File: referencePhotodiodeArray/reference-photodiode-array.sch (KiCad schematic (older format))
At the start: 18 parts

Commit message: fix reference photodiode array
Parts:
- D1, D2, D3, D4, D5, D6, D7, D8: footprint Diodes_ThroughHole:D_T-1_P5.08mm_Horizontal -> testPad:BPW34
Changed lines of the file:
@@
 F 0 "D2" H 2420 2370 50  0000 L CNN
 F 1 "D_Photo" H 2360 2190 50  0000 C CNN
-F 2 "Diodes_ThroughHole:D_T-1_P5.08mm_Horizontal" H 2350 2300 50  0001 C CNN
+F 2 "testPad:BPW34" H 2350 2300 50  0001 C CNN
 F 3 "" H 2350 2300 50  0000 C CNN
 	1    2400 2300
@@
 F 0 "D3" H 2870 1670 50  0000 L CNN
 F 1 "D_Photo" H 2810 1490 50  0000 C CNN
-F 2 "Diodes_ThroughHole:D_T-1_P5.08mm_Horizontal" H 2800 1600 50  0001 C CNN
+F 2 "testPad:BPW34" H 2800 1600 50  0001 C CNN
 F 3 "" H 2800 1600 50  0000 C CNN
 	1    2850 1600
@@
 F 0 "D1" H 2420 1670 50  0000 L CNN
 F 1 "D_Photo" H 2360 1490 50  0000 C CNN
-F 2 "Diodes_ThroughHole:D_T-1_P5.08mm_Horizontal" H 2350 1600 50  0001 C CNN
+F 2 "testPad:BPW34" H 2350 1600 50  0001 C CNN
 F 3 "" H 2350 1600 50  0000 C CNN
 	1    2400 1600
@@
 F 0 "D5" H 3320 1670 50  0000 L CNN
 F 1 "D_Photo" H 3260 1490 50  0000 C CNN
-F 2 "Diodes_ThroughHole:D_T-1_P5.08mm_Horizontal" H 3250 1600 50  0001 C CNN
+F 2 "testPad:BPW34" H 3250 1600 50  0001 C CNN
 F 3 "" H 3250 1600 50  0000 C CNN
 	1    3300 1600
@@
 F 0 "D7" H 3770 1670 50  0000 L CNN
 F 1 "D_Photo" H 3710 1490 50  0000 C CNN
-F 2 "Diodes_ThroughHole:D_T-1_P5.08mm_Horizontal" H 3700 1600 50  0001 C CNN
+F 2 "testPad:BPW34" H 3700 1600 50  0001 C CNN
 F 3 "" H 3700 1600 50  0000 C CNN
 	1    3750 1600
@@
 F 0 "D4" H 2870 2370 50  0000 L CNN
 F 1 "D_Photo" H 2810 2190 50  0000 C CNN
-F 2 "Diodes_ThroughHole:D_T-1_P5.08mm_Horizontal" H 2800 2300 50  0001 C CNN
+F 2 "testPad:BPW34" H 2800 2300 50  0001 C CNN
 F 3 "" H 2800 2300 50  0000 C CNN
 	1    2850 2300
@@
 F 0 "D6" H 3320 2370 50  0000 L CNN
 F 1 "D_Photo" H 3260 2190 50  0000 C CNN
-F 2 "Diodes_ThroughHole:D_T-1_P5.08mm_Horizontal" H 3250 2300 50  0001 C CNN
+F 2 "testPad:BPW34" H 3250 2300 50  0001 C CNN
 F 3 "" H 3250 2300 50  0000 C CNN
 	1    3300 2300
@@
 F 0 "D8" H 3770 2370 50  0000 L CNN
 F 1 "D_Photo" H 3710 2190 50  0000 C CNN
-F 2 "Diodes_ThroughHole:D_T-1_P5.08mm_Horizontal" H 3700 2300 50  0001 C CNN
+F 2 "testPad:BPW34" H 3700 2300 50  0001 C CNN
 F 3 "" H 3700 2300 50  0000 C CNN
 	1    3750 2300

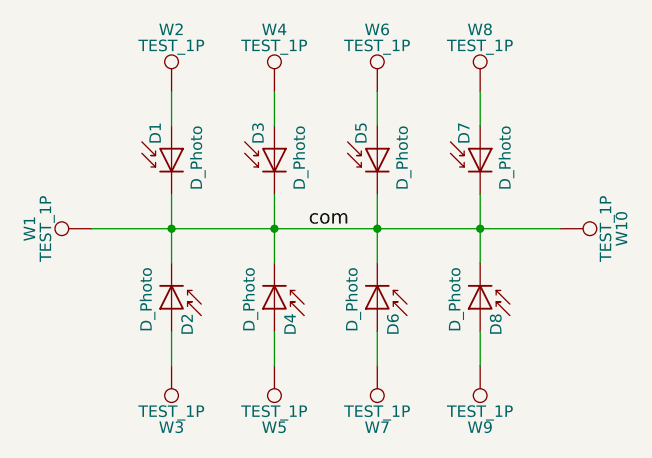
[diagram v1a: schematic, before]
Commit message: put pads on both sides
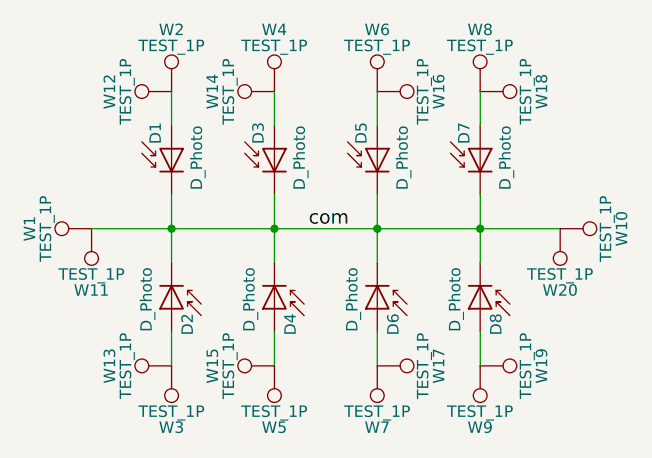
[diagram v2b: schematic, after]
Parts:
- added W11, W12, W13, W14, W15, W16, W17, W18, W19, W20: TEST_1P, testPad:SolderWirePad_single_SMD_5x2.3mm, symbol TEST_1P
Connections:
- net com: now also W11.1, W20.1
- net at D2.2 (A), W3.1: now also W13.1
- net at D3.2 (A), W4.1: now also W14.1
- net at D1.2 (A), W2.1: now also W12.1
- net at D5.2 (A), W6.1: now also W16.1
- net at D7.2 (A), W8.1: now also W18.1
- net at D4.2 (A), W5.1: now also W15.1
- net at D6.2 (A), W7.1: now also W17.1
- net at D8.2 (A), W9.1: now also W19.1
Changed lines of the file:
@@
 Text Label 3000 1950 0    60   ~ 0
 com
+$Comp
+L TEST_1P W12
+U 1 1 58C6E544
+P 2400 1350
+F 0 "W12" H 2400 1620 50  0000 C CNN
+F 1 "TEST_1P" H 2400 1550 50  0000 C CNN
+F 2 "testPad:SolderWirePad_single_SMD_5x2.3mm" H 2600 1350 50  0001 C CNN
+F 3 "" H 2600 1350 50  0000 C CNN
+	1    2400 1350
+	0    -1   -1   0
+$EndComp
+$Comp
+L TEST_1P W14
+U 1 1 58C6E5BF
+P 2850 1350
+F 0 "W14" H 2850 1620 50  0000 C CNN
+F 1 "TEST_1P" H 2850 1550 50  0000 C CNN
+F 2 "testPad:SolderWirePad_single_SMD_5x2.3mm" H 3050 1350 50  0001 C CNN
+F 3 "" H 3050 1350 50  0000 C CNN
+	1    2850 1350
+	0    -1   -1   0
+$EndComp
+$Comp
+L TEST_1P W16
+U 1 1 58C6E61B
+P 3300 1350
+F 0 "W16" H 3300 1620 50  0000 C CNN
+F 1 "TEST_1P" H 3300 1550 50  0000 C CNN
+F 2 "testPad:SolderWirePad_single_SMD_5x2.3mm" H 3500 1350 50  0001 C CNN
+F 3 "" H 3500 1350 50  0000 C CNN
+	1    3300 1350
+	0    1    1    0
+$EndComp
+$Comp
+L TEST_1P W18
+U 1 1 58C6E66E
+P 3750 1350
+F 0 "W18" H 3750 1620 50  0000 C CNN
+F 1 "TEST_1P" H 3750 1550 50  0000 C CNN
+F 2 "testPad:SolderWirePad_single_SMD_5x2.3mm" H 3950 1350 50  0001 C CNN
+F 3 "" H 3950 1350 50  0000 C CNN
+	1    3750 1350
+	0    1    1    0
+$EndComp
+$Comp
+L TEST_1P W19
+U 1 1 58C6E6C6
+P 3750 2550
+F 0 "W19" H 3750 2820 50  0000 C CNN
+F 1 "TEST_1P" H 3750 2750 50  0000 C CNN
+F 2 "testPad:SolderWirePad_single_SMD_5x2.3mm" H 3950 2550 50  0001 C CNN
+F 3 "" H 3950 2550 50  0000 C CNN
+	1    3750 2550
+	0    1    1    0
+$EndComp
+$Comp
+L TEST_1P W17
+U 1 1 58C6E721
+P 3300 2550
+F 0 "W17" H 3300 2820 50  0000 C CNN
+F 1 "TEST_1P" H 3300 2750 50  0000 C CNN
+F 2 "testPad:SolderWirePad_single_SMD_5x2.3mm" H 3500 2550 50  0001 C CNN
+F 3 "" H 3500 2550 50  0000 C CNN
+	1    3300 2550
+	0    1    1    0
+$EndComp
+$Comp
+L TEST_1P W15
+U 1 1 58C6E77F
+P 2850 2550
+F 0 "W15" H 2850 2820 50  0000 C CNN
+F 1 "TEST_1P" H 2850 2750 50  0000 C CNN
+F 2 "testPad:SolderWirePad_single_SMD_5x2.3mm" H 3050 2550 50  0001 C CNN
+F 3 "" H 3050 2550 50  0000 C CNN
+	1    2850 2550
+	0    -1   -1   0
+$EndComp
+$Comp
+L TEST_1P W13
+U 1 1 58C6E7F5
+P 2400 2550
+F 0 "W13" H 2400 2820 50  0000 C CNN
+F 1 "TEST_1P" H 2400 2750 50  0000 C CNN
+F 2 "testPad:SolderWirePad_single_SMD_5x2.3mm" H 2600 2550 50  0001 C CNN
+F 3 "" H 2600 2550 50  0000 C CNN
+	1    2400 2550
+	0    -1   -1   0
+$EndComp
+$Comp
+L TEST_1P W11
+U 1 1 58C6E855
+P 2050 1950
+F 0 "W11" H 2050 2220 50  0000 C CNN
+F 1 "TEST_1P" H 2050 2150 50  0000 C CNN
+F 2 "testPad:SolderWirePad_single_SMD_5x2.3mm" H 2250 1950 50  0001 C CNN
+F 3 "" H 2250 1950 50  0000 C CNN
+	1    2050 1950
+	-1   0    0    1
+$EndComp
+$Comp
+L TEST_1P W20
+U 1 1 58C6E8BA
+P 4100 1950
+F 0 "W20" H 4100 2220 50  0000 C CNN
+F 1 "TEST_1P" H 4100 2150 50  0000 C CNN
+F 2 "testPad:SolderWirePad_single_SMD_5x2.3mm" H 4300 1950 50  0001 C CNN
+F 3 "" H 4300 1950 50  0000 C CNN
+	1    4100 1950
+	-1   0    0    1
+$EndComp
 $EndSCHEMATC
